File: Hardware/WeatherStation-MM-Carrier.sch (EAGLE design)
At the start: 73 parts, among them J11 microSD, J13 RJ11 - WIND, J2 JTAG, J3 QWIIC_RIGHT_ANGLE, J7 RJ11 - RAIN, J9 MICROMOD-2222-C, U1 BME280, U2 VEML6075, U5 AP7361C-33FGE

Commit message: Fix net names
Also renamed the sch/brd files to the right name
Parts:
- removed JP3: EN ADR PU, SparkFun-Jumpers:JUMPER-SMT_3_1-NC_TRACE_SILK
- removed R7: 4.7k, SparkFun-Resistors:4.7KOHM-0603-1/10W-1%
- added C6: 1.0uF, SparkFun-Capacitors:1.0UF-0603-16V-10%
- added C7: 10uF, SparkFun-Capacitors:10UF-0603-6.3V-20%
- added C8: 1nF, SparkFun-Capacitors:1.0NF/1000PF-0603-50V-10%
- added D11: Yellow, SparkFun-LED:LED-YELLOW0603
- added JP2: VIN LED ENABLE, SparkFun-Jumpers:JUMPER-SMT_2_NC_TRACE_SILK
- added L1: 100uH, SparkFun-Coils:MA5532-AE
- added R19, R6: 10k, SparkFun-Resistors:10KOHM-0603-1/10W-1%
- added R20: 1k, SparkFun-Resistors:1KOHM-0603-1/10W-1%
- added R21: 4.7k, SparkFun-Resistors:4.7KOHM-0603-1/10W-1%
- added U3: AS3935, SparkFun-Sensors:AS3935QFN
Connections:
- removed net CAMERA_D0: J9.G0
- removed net CAMERA_D1: J9.G1
- removed net CAMERA_D2: J9.G2
- removed net CAMERA_D3: J9.G3
- removed net CAMERA_D4: J9.G4
- removed net CAMERA_D5: J9.G5
- removed net CAMERA_D6: J9.G6
- removed net CAMERA_D7: J9.G7
- removed net CAMERA_HSYNC: J9.G10/ADC_D+
- removed net CAMERA_I2C_SCL: J9.I2C_SCL1
- removed net CAMERA_I2C_SDA: J9.I2C_SDA1
- removed net CAMERA_INT: J9.I2C_!INT!
- removed net CAMERA_MCLK: J9.AUD_MCLK/CLKOUT
- removed net CAMERA_PCLK: J9.AUD_OUT
- removed net CAMERA_TRIG: J9.G8
- removed net CAMERA_VSYNC: J9.G9/ADC_D-
- removed net I2S_SCK/PDM_CLK: J9.AUD_CLK
- removed net I2S_SD: J9.AUD_IN
- removed net I2S_WS/PDM_DAT: J9.AUD_DATA
- removed net N$8: JP3.3, R7.1
- removed net USBHOST_D+: J9.USBHOST_D+
- removed net USBHOST_D-: J9.USBHOST_D-
- new net INP: C8.1, L1.1, R6.2, U3.INP
- new net LIGHTNING_INT: J9.G0, U3.IRQ
- new net N$15: C7.1, U3.AC_GND
- new net N$16: D11.A, R20.1
- new net N$19: R21.1, U1.!CS
- new net N$5: JP2.1, R20.2
- net 3.3V: now also C6.1, R19.2, R21.2, U3.VDD, U3.VREG; no longer R7.2, U1.!CS
- net A0: no longer J9.A0
- net A1: no longer J9.A1
- net BME_ADR: no longer JP3.2
- net D0: no longer J9.D0
- net D1: no longer J9.D1
- net GND: now also C6.2, C7.2, C8.2, D11.C, L1.2, R6.1, U3.ADD0, U3.ADD1, U3.EN_VREG, U3.GND, U3.GND_PAD, U3.INN, U3.SI; no longer JP3.1
- net PWM0: no longer J9.PWM0
- net PWM1: no longer J9.PWM1
- net RAIN: now also J9.G2
- net RX1: no longer J9.RX1
- net RX2: no longer J9.RX2
- net SOIL_MOIST_SIG: now also J9.A0
- net SPI_!CS!: now also R19.1, U3.!CS
- net SPI_CLK: now also U3.SCL/I2CL
- net SPI_MISO: now also U3.MISO
- net SPI_MOSI: now also U3.MOSI/I2CD
- net TX1: no longer J9.TX1
- net TX2: no longer J9.TX2
- net VIN: now also JP2.2
- net WDIR: now also J9.A1
- net WSPEED: now also J9.G1
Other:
- note added: "Default address: 0x76 NOTE: address can be changed in software"
- note added: "I2C Mode ADR: 0x76"
- note added: "I2C address: 0x10"
- note added: "LED's"
- note added: "Lightning Detector"
- moved on the sheet: BT1, BYP, C1, C13, C2, C3, C4, D1, D2, D6, D7, F2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

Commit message: Final schematic changes from review and Nate's notes
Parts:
- removed D10, D3, D4, D5, D8, D9: 250mA/100V, SparkFun-DiscreteSemi:DIODE-BAS16J
- removed R15, R16, R17: 1k, SparkFun-Resistors:1KOHM-0603-1/10W-1%
- removed R18: 4.7k, SparkFun-Resistors:4.7KOHM-0603-1/10W-1%
- added C10: 1.0uF, SparkFun-Capacitors:1.0UF-0603-16V-10%
- added C11: 0.22uF, SparkFun-Capacitors:0.22UF-0603-25V-10%
- added C12, C14: 0.1uF, SparkFun-Capacitors:0.1UF-0603-25V-(+80/-20%)
- added C9: 10uF, SparkFun-Capacitors:10UF-0603-6.3V-20%
- added R7: 10k, SparkFun-Resistors:10KOHM-0603-1/10W-1%
- JP2: value VIN LED ENABLE -> VIN LED
- JP4: value 3V3 LED ENABLE -> 3V3 LED
- R12, R13, R14: value 1k -> 10k; device SparkFun-Resistors:1KOHM-0603-1/10W-1% -> SparkFun-Resistors:10KOHM-0603-1/10W-1%
- R21: value 4.7k -> 10k; device SparkFun-Resistors:4.7KOHM-0603-1/10W-1% -> SparkFun-Resistors:10KOHM-0603-1/10W-1%
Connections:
- removed net 5V: D10.C, D3.C, D9.C, R18.2
- removed net BME_ADR: U1.SDO/ADR
- removed net N$12: J13.5, R14.1
- removed net N$13: J13.4, R15.1
- removed net N$17: J13.3, R16.1
- removed net N$18: J13.2, R17.1
- removed net N$7: J7.4, R12.2
- removed net N$9: J7.3, R13.2
- removed net RAIN2: J7.2
- removed net RAIN5: J7.5
- new net N$8: R7.1, U1.SDO/ADR
- new net SOIL_MOIST_PWR: J4.1, J9.G3
- net 3.3V: now also R12.2, R13.2, R14.2, R7.2; no longer J4.1
- net GND: now also C10.2, C11.2, C12.2, C14.2, C9.2; no longer D4.A, D5.A, D8.A, R12.1, R14.2, R15.2
- net N$1: now also C10.1, C11.1, C9.1
- net RAIN: now also C12.1, J7.3, R12.1; no longer D3.A, D4.C, R13.1
- net WDIR: now also J13.2, R14.1; no longer D5.C, D9.A, R17.2, R18.1
- net WSPEED: now also C14.1, J13.3, R13.1; no longer D10.A, D8.C, R16.2
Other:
- note added: "Default address: 0x77"
- note added: "I2C Mode"
- note added: "LEDs"
- note added: "Select SPI mode"
- note added: "Soil Moisture Sensor Connector"
- note removed: "Default address: 0x76 NOTE: address can be changed in software"
- note removed: "I2C Mode ADR: 0x76"
- note removed: "LED's"
- note removed: "Soil Mositure Sensor Connector"
- moved on the sheet: C1, C13, C2, C3, C4, D1, D11, D2, J13, J7, JP2, JP4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

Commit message: Preliminary board layout
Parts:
- removed C12, C14: 0.1uF, SparkFun-Capacitors:0.1UF-0603-25V-(+80/-20%)
- removed LOGO1: SFE_LOGO_NAME_FLAME.1_INCH, SparkFun-Aesthetics:SFE_LOGO_NAME_FLAME.1_INCH
- added D10, D3, D4, D5, D8, D9: 250mA/100V, SparkFun-DiscreteSemi:DIODE-BAS16J
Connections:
- removed net A0: J8.1
- removed net A1: J8.2
- net 3.3V: now also D3.C, D5.C, D9.C
- net D0: now also J9.D0
- net D1: now also J9.D1
- net GND: now also D10.A, D4.A, D8.A, J13.4, J13.5, J7.4; no longer C12.2, C14.2
- net PWM0: now also J9.PWM0
- net PWM1: now also J9.PWM1
- net RAIN: now also D3.A, D4.C; no longer C12.1
- net RX1: now also J9.RX1
- net RX2: now also J9.RX2
- net SOIL_MOIST_SIG: now also J8.1
- net TX1: now also J9.TX1
- net TX2: now also J9.TX2
- net WDIR: now also D10.C, D9.A, J8.2
- net WSPEED: now also D5.A, D8.C; no longer C14.1
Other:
- moved on the sheet: R12, R13, R14

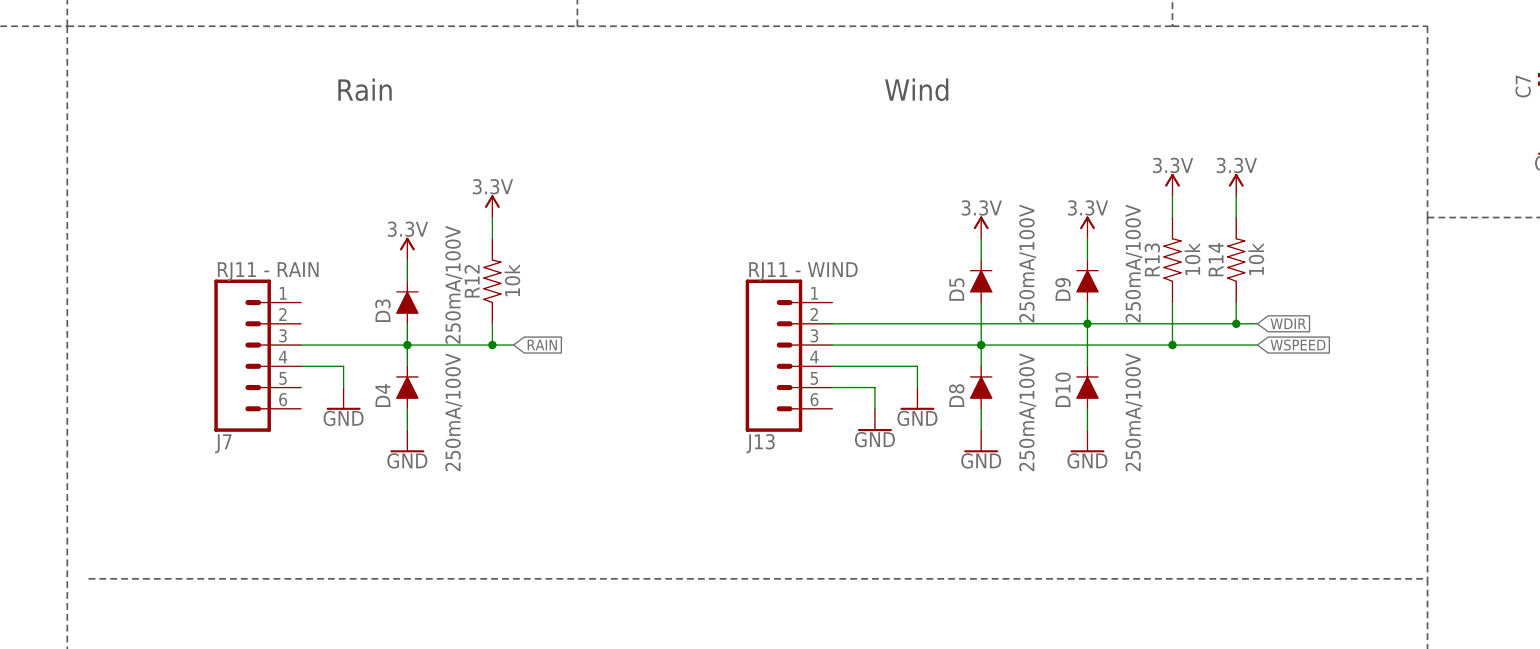
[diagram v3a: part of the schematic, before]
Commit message: Revised hardware layout
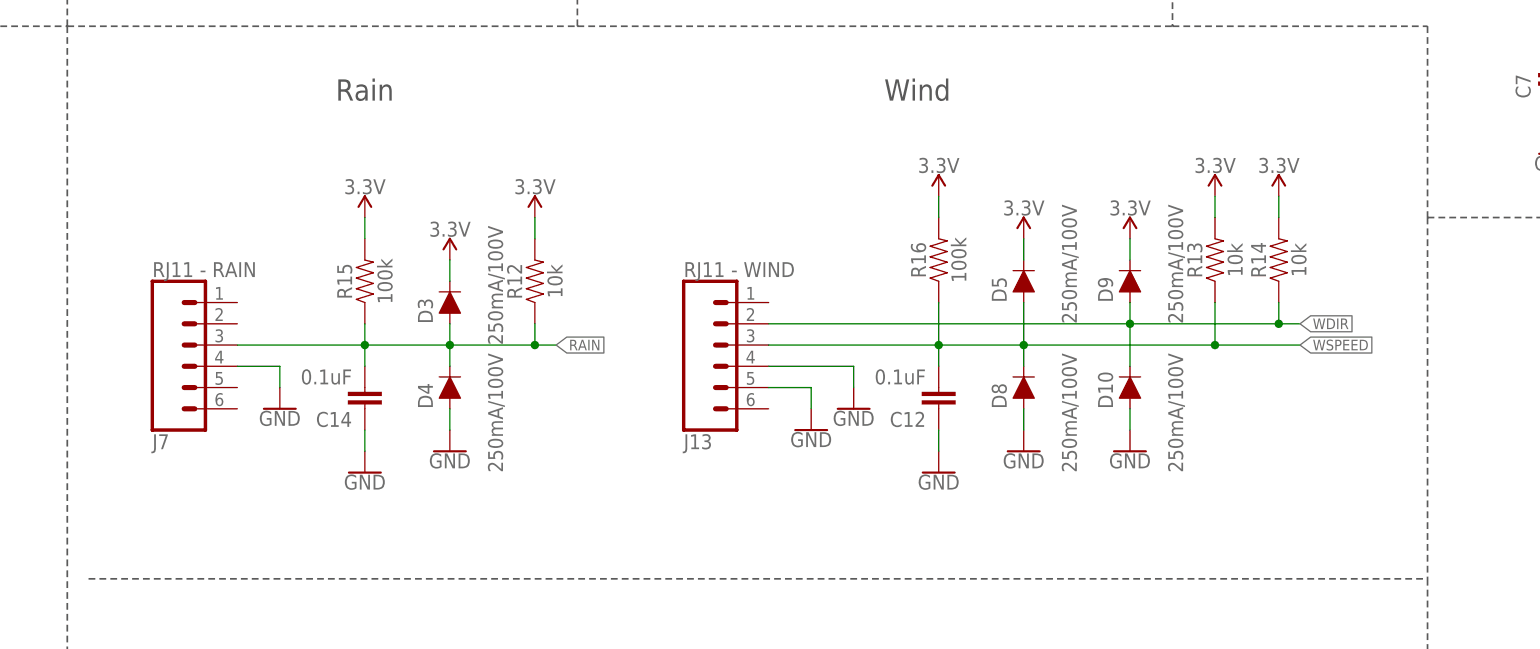
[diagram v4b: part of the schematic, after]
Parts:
- added C12, C14: 0.1uF, SparkFun-Capacitors:0.1UF-0603-25V-(+80/-20%)
- added R15, R16: 100k, SparkFun-Resistors:100KOHM-0603-1/10W-1%
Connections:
- net 3.3V: now also R15.2, R16.2
- net GND: now also C12.1, C14.1
- net RAIN: now also C14.2, R15.1
- net WSPEED: now also C12.2, R16.1
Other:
- moved on the sheet: D10, D3, D4, D5, D8, D9, J13, J7, R12, R13, R14

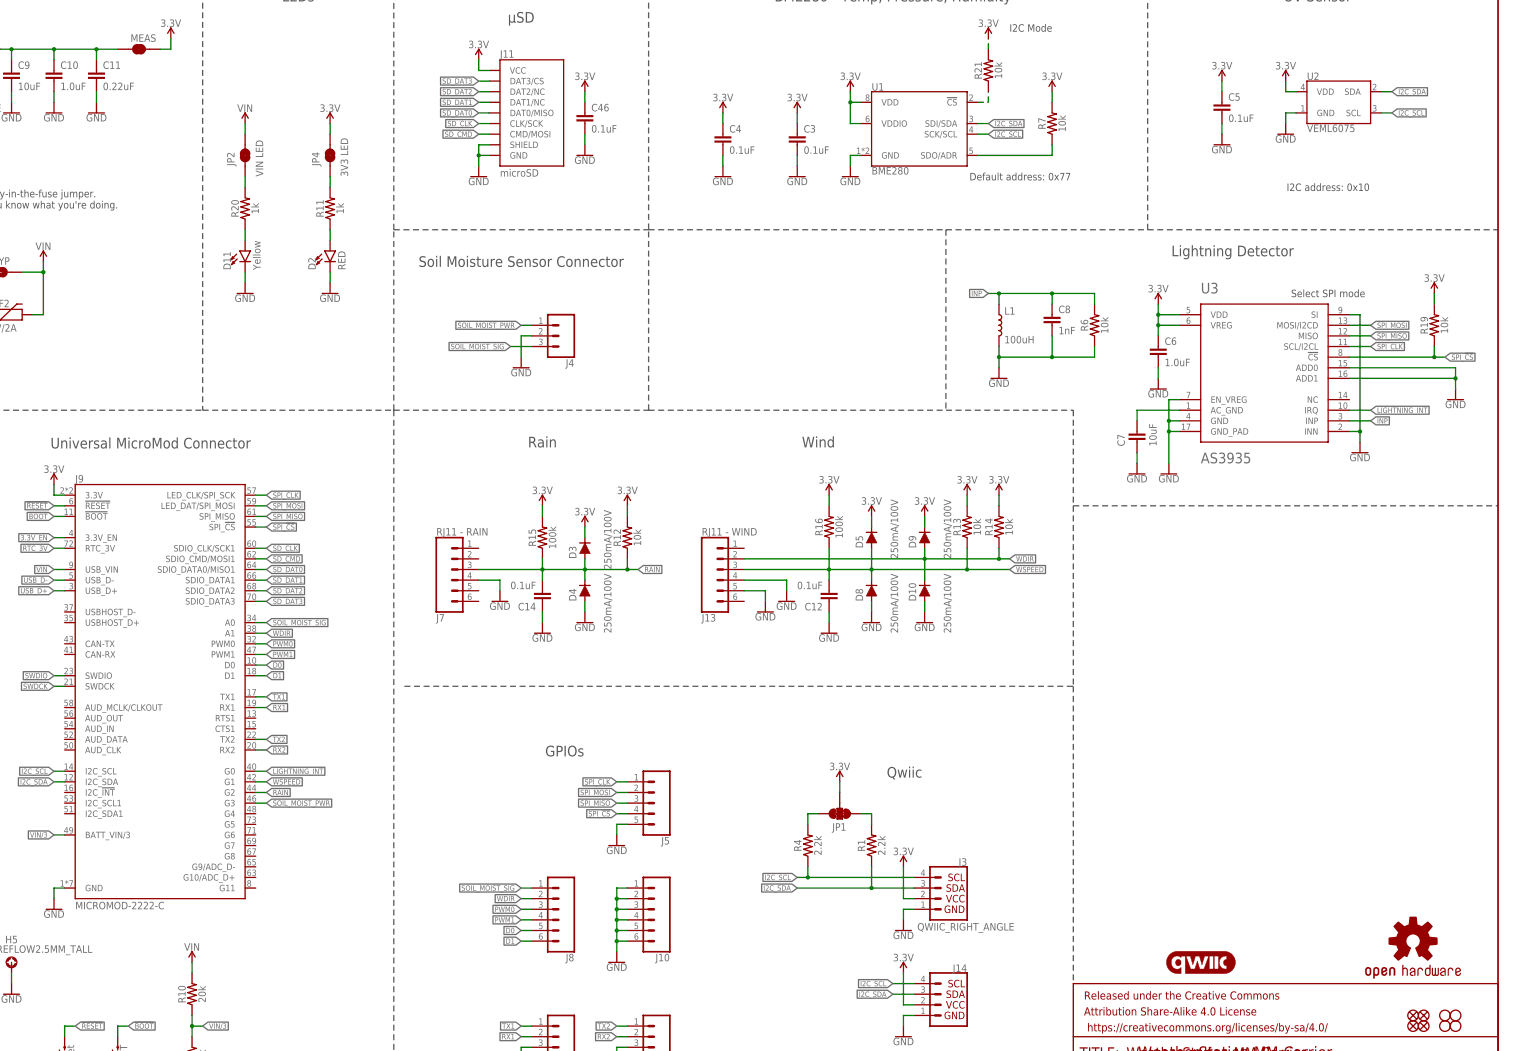
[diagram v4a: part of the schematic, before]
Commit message: Change MM pinout to new SPI standard
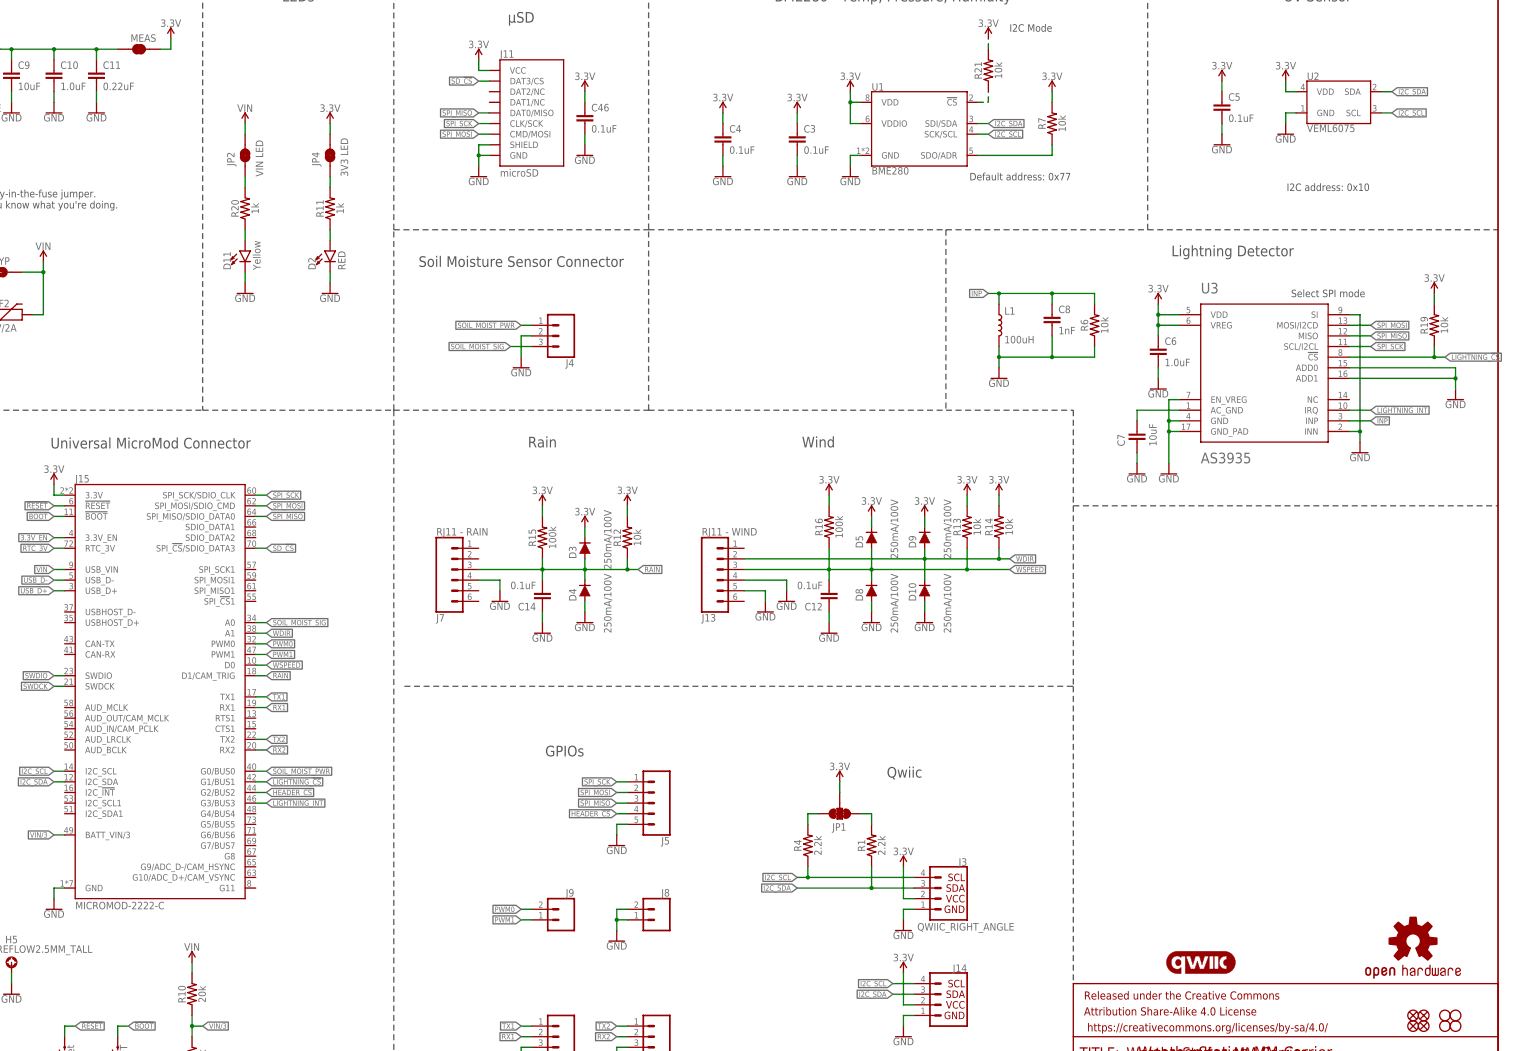
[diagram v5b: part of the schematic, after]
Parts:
- removed J10: (no value), SparkFun-Connectors:CONN_06NO_SILK_NO_POP
- added J15: MICROMOD-2222-C, SparkFun-MicroMod:MICROMOD-2222-C
- J8: device SparkFun-Connectors:CONN_06NO_SILK_NO_POP -> SparkFun-Connectors:CONN_021X02_NO_SILK
- J9: value MICROMOD-2222-C -> (none); device Teensy:MICROMOD-2222-C -> SparkFun-Connectors:CONN_021X02_NO_SILK
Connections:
- removed net D0: J8.5, J9.D0
- removed net D1: J8.6, J9.D1
- removed net SD_CLK: J11.CLK/SCK, J9.SDIO_CLK/SCK1
- removed net SD_CMD: J11.CMD/MOSI, J9.SDIO_CMD/MOSI1
- removed net SD_DAT0: J11.DAT0/MISO, J9.SDIO_DATA0/MISO1
- removed net SD_DAT1: J11.DAT1/NC, J9.SDIO_DATA1
- removed net SD_DAT2: J11.DAT2/NC, J9.SDIO_DATA2
- removed net SD_DAT3: J11.DAT3/CS, J9.SDIO_DATA3
- removed net SPI_!CS!: J5.4, J9.SPI_!CS!, R19.1, U3.!CS
- removed net SPI_CLK: J5.1, J9.LED_CLK/SPI_SCK, U3.SCL/I2CL
- new net HEADER_!CS!: J15.G2/BUS2, J5.4
- new net LIGHTNING_!CS!: J15.G1/BUS1, R19.1, U3.!CS
- new net SD_!CS!: J11.DAT3/CS, J15.SPI_!CS!/SDIO_DATA3
- new net SPI_SCK: J11.CLK/SCK, J15.SPI_SCK/SDIO_CLK, J5.1, U3.SCL/I2CL
- net !BOOT!: now also J15.!BOOT!; no longer J9.!BOOT!
- net !RESET!: now also J15.!RESET!; no longer J9.!RESET!
- net 3.3V: now also J15.3.3V; no longer J9.3.3V
- net 3.3V_EN: now also J15.3.3V_EN; no longer J9.3.3V_EN
- net GND: now also J15.GND, J8.1, J8.2; no longer J10.1, J10.2, J10.3, J10.4, J10.5, J10.6, J9.GND
- net I2C_SCL: now also J15.I2C_SCL; no longer J9.I2C_SCL
- net I2C_SDA: now also J15.I2C_SDA; no longer J9.I2C_SDA
- net LIGHTNING_INT: now also J15.G3/BUS3; no longer J9.G0
- net PWM0: now also J15.PWM0, J9.2; no longer J8.3, J9.PWM0
- net PWM1: now also J15.PWM1, J9.1; no longer J8.4, J9.PWM1
- net RAIN: now also J15.D1/CAM_TRIG; no longer J9.G2
- net RTC_3V: now also J15.RTC_3V; no longer J9.RTC_3V
- net RX1: now also J15.RX1; no longer J9.RX1
- net RX2: now also J15.RX2; no longer J9.RX2
- net SOIL_MOIST_PWR: now also J15.G0/BUS0; no longer J9.G3
- net SOIL_MOIST_SIG: now also J15.A0; no longer J8.1, J9.A0
- net SPI_MISO: now also J11.DAT0/MISO, J15.SPI_MISO/SDIO_DATA0; no longer J9.SPI_MISO
- net SPI_MOSI: now also J11.CMD/MOSI, J15.SPI_MOSI/SDIO_CMD; no longer J9.LED_DAT/SPI_MOSI
- net SWDCK: now also J15.SWDCK; no longer J9.SWDCK
- net SWDIO: now also J15.SWDIO; no longer J9.SWDIO
- net TX1: now also J15.TX1; no longer J9.TX1
- net TX2: now also J15.TX2; no longer J9.TX2
- net USB_D+: now also J15.USB_D+; no longer J9.USB_D+
- net USB_D-: now also J15.USB_D-; no longer J9.USB_D-
- net VIN: now also J15.USB_VIN; no longer J9.USB_VIN
- net VIN/3: now also J15.BATT_VIN/3; no longer J9.BATT_VIN/3
- net WDIR: now also J15.A1; no longer J8.2, J9.A1
- net WSPEED: now also J15.D0; no longer J9.G1

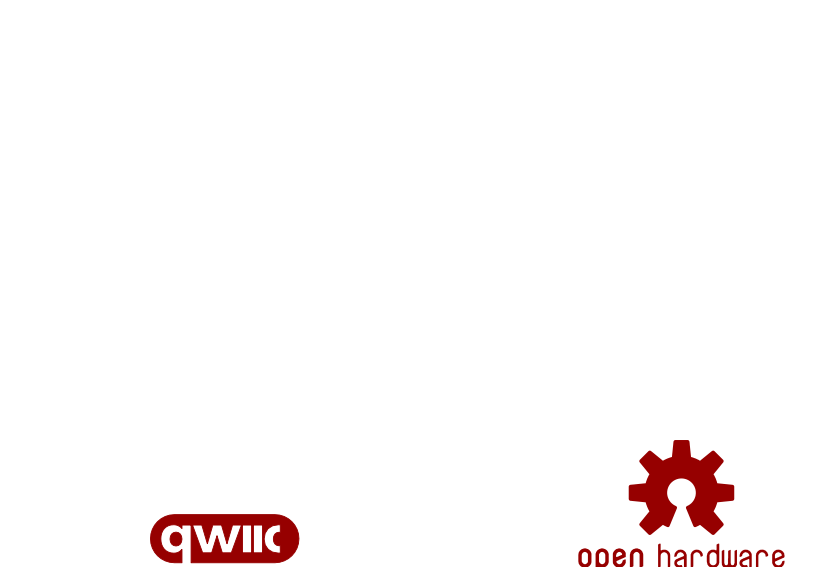
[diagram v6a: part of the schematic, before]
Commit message: Added silkscreen
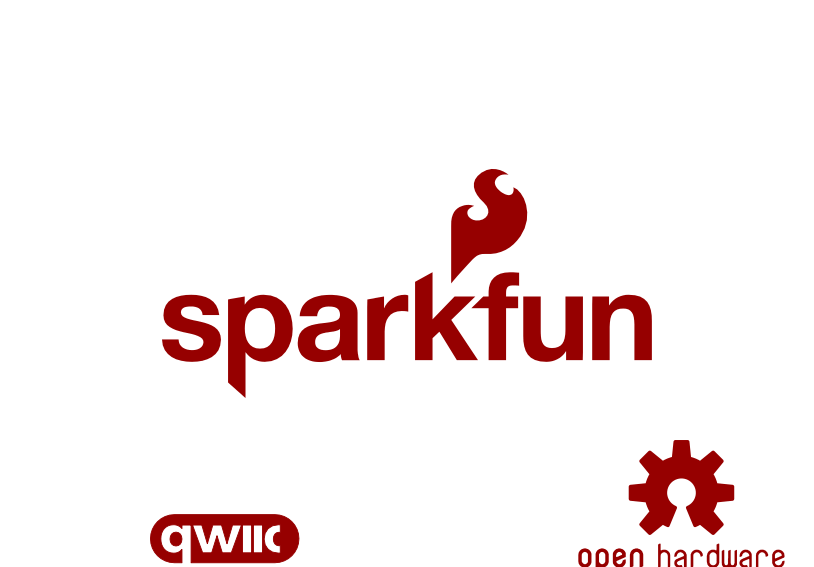
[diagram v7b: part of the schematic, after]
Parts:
- added LOGO1: SFE_LOGO_NAME_FLAME.2_INCH, SparkFun-Aesthetics:SFE_LOGO_NAME_FLAME.2_INCH
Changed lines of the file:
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@@
 <part name="J8" library="SparkFun-Connectors" deviceset="CONN_02" device="1X02_NO_SILK"/>
 <part name="J9" library="SparkFun-Connectors" deviceset="CONN_02" device="1X02_NO_SILK"/>
+<part name="LOGO1" library="SparkFun-Aesthetics" deviceset="SFE_LOGO_NAME_FLAME" device=".2_INCH"/>
 </parts>
 <sheets>
@@
 <attribute name="NAME" x="210.82" y="56.388" size="1.778" layer="95" font="vector" rot="MR0"/>
 </instance>
+<instance part="LOGO1" gate="G$1" x="353.06" y="55.88" smashed="yes"/>
 </instances>
 <busses>
